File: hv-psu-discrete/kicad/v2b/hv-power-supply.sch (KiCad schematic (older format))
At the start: 86 parts, among them J1 AC-HV, J10 GND_LV, J11 EARTH, J12 AC-LV, J13 AC-LV, J2 AC-HV, J3 HV, J4 GND_HV, J5 LV, J6 GND_LV, J7 LED, J8 GND_LV, J9 +5V, Q1 LND150N3-G, Q2 IRF840, Q3 MMBT3904, U1 LT3080xT, U2 LM317_TO-220, U3 LM7805_TO220, U4 TLC555xD

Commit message: WIP
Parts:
- removed C8, C9: 10nF/50V, Capacitor_SMD:C_0805_2012Metric_Pad1.18x1.45mm_HandSolder, symbol Device:C
- removed D1: BYG20J, Diode_SMD:D_SMA_Handsoldering, symbol Device:D
- removed D14: 1N4148W, Diode_SMD:D_SOD-123, symbol Diode:1N4148W
- removed RL1: G2RL-2-DC5, Relay_THT:Relay_DPDT_Omron_G2RL, symbol Relay:G2RL-2-DC5
- removed U1: LT3080xT, Package_TO_SOT_THT:TO-220-5_P3.4x3.7mm_StaggerOdd_Lead3.8mm_Vertical, symbol Regulator_Linear:LT3080xT
- added D1: 1N4148W, Diode_SMD:D_SOD-123, symbol Diode:1N4148W
- added D14: BYG20J, Diode_SMD:D_SMA_Handsoldering, symbol Device:D
- added D17, D18: 1N4007, Diode_SMD:D_SMA_Handsoldering, symbol Diode:1N4007
- added K1: G6S-2 DC5, Relay_THT:Relay_DPDT_Omron_G6S-2, symbol Relay:G6S-2
- added R19: Rs/2W, Resistor_THT:R_Axial_DIN0414_L11.9mm_D4.5mm_P15.24mm_Horizontal, symbol Device:R
- added R20: Rs/0.6W, Resistor_THT:R_Axial_DIN0207_L6.3mm_D2.5mm_P10.16mm_Horizontal, symbol Device:R
- added R21, R22: 100k/2W, Resistor_THT:R_Axial_DIN0414_L11.9mm_D4.5mm_P15.24mm_Horizontal, symbol Device:R
- added U1: LT3080xST, Package_TO_SOT_SMD:SOT-223, symbol Regulator_Linear:LT3080xST
- C1: value 2.2nF/2kV -> Cx/10nF/50V; footprint Capacitor_THT:C_Rect_L18.0mm_W5.0mm_P15.00mm_FKS3_FKP3 -> Capacitor_SMD:C_0805_2012Metric_Pad1.18x1.45mm_HandSolder
- C14: footprint Capacitor_THT:CP_Radial_D30.0mm_P10.00mm_SnapIn -> Capacitor_THT:CP_Radial_D35.0mm_P10.00mm_SnapIn
- C2: value 10nF/630VDC -> 2.2nF 2kV; footprint Capacitor_THT:C_Rect_L13.0mm_W4.0mm_P10.00mm_FKS3_FKP3_MKS4 -> Capacitor_THT:C_Rect_L18.0mm_W5.0mm_P15.00mm_FKS3_FKP3
- C20: footprint Capacitor_Tantalum_SMD:CP_EIA-7343-31_Kemet-D_Pad2.25x2.55mm_HandSolder -> Capacitor_Tantalum_SMD:CP_EIA-3216-12_Kemet-S_Pad1.58x1.35mm_HandSolder
- C3: value 10nF/630VDC -> Cs/50V; footprint Capacitor_THT:C_Rect_L13.0mm_W4.0mm_P10.00mm_FKS3_FKP3_MKS4 -> Capacitor_SMD:C_0805_2012Metric_Pad1.18x1.45mm_HandSolder
- C4: value 10nF/50V -> Cx/10nF/630V; footprint Capacitor_SMD:C_0805_2012Metric_Pad1.18x1.45mm_HandSolder -> Capacitor_THT:C_Rect_L13.0mm_W4.0mm_P10.00mm_FKS3_FKP3_MKS4
- C5: value 10nF/50V -> Cs/630V; footprint Capacitor_SMD:C_0805_2012Metric_Pad1.18x1.45mm_HandSolder -> Capacitor_THT:C_Rect_L18.0mm_W5.0mm_P15.00mm_FKS3_FKP3
- C6: value 10nF/630VDC -> 100nF/50V; footprint Capacitor_THT:C_Rect_L13.0mm_W4.0mm_P10.00mm_FKS3_FKP3_MKS4 -> Capacitor_SMD:C_0805_2012Metric_Pad1.18x1.45mm_HandSolder
- C7: value 10nF/630VDC -> 100nF/630V; footprint Capacitor_THT:C_Rect_L13.0mm_W4.0mm_P10.00mm_FKS3_FKP3_MKS4 -> Capacitor_THT:C_Rect_L18.0mm_W5.0mm_P15.00mm_FKS3_FKP3
- D10, D9: value 1N4736A/6.3V -> MMSZ5234BT1G/6.2V; footprint Diode_THT:D_DO-41_SOD81_P10.16mm_Horizontal -> Diode_SMD:D_SOD-123
- D11, D15: footprint Diode_THT:D_DO-41_SOD81_P10.16mm_Horizontal -> Diode_SMD:D_SMA_Handsoldering
- D12: value 1N4007 -> 1N4148W; footprint Diode_THT:D_DO-41_SOD81_P10.16mm_Horizontal -> Diode_SMD:D_SOD-123
- D16: value 1N4747A/20V -> MMSZ20T1G/20V; footprint Diode_THT:D_DO-41_SOD81_P10.16mm_Horizontal -> Diode_SMD:D_SOD-123
- D2, D5: value BYG20J -> BYG22B-E3
- D3, D4: value BYV98-200 -> BYG22B-E3; footprint kicad-snk:SOD64-10 -> Diode_SMD:D_SMA_Handsoldering
- D7, D8: value BYV98-200 -> BYG20J; footprint kicad-snk:SOD64-10 -> Diode_SMD:D_SMA_Handsoldering
- HS1: footprint Heatsink:Heatsink_Fischer_SK104-STC-STIC_35x13mm_2xDrill2.5mm -> Heatsink:Heatsink_Fischer_SK129-STS_42x25mm_2xDrill2.5mm
- J1, J2: value AC-HV -> AC-LV
- J11: value EARTH -> AC-HV
- J12: value AC-LV -> AC-HV
- J13: value AC-LV -> EARTH
- Q1: footprint Package_TO_SOT_THT:TO-92 -> Package_TO_SOT_SMD:SOT-89-3_Handsoldering
- R1: value 100R/2W -> Rs/1/8W; footprint Resistor_THT:R_Axial_DIN0411_L9.9mm_D3.6mm_P15.24mm_Horizontal -> Resistor_SMD:R_0805_2012Metric_Pad1.20x1.40mm_HandSolder
- R18: footprint Resistor_THT:R_Axial_DIN0411_L9.9mm_D3.6mm_P15.24mm_Horizontal -> Resistor_THT:R_Axial_DIN0414_L11.9mm_D4.5mm_P15.24mm_Horizontal
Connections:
- net GND_HV: now also C7.2, D6.2 (A), D7.2 (A), R18.2, D18.2 (A), R21.2, R22.2; no longer C1.1, C3.1, D2.2 (A), R1.1
- net GND_LV: now also C6.2, D2.2 (A); no longer C4.2, C5.1, D4.2 (A)
- net at C4.1, J12.1 (Pin_1): now also K1.8, R19.2; no longer D3.1 (K), D7.2 (A)
- net at C14.1, C15.1, C16.1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: now also D4.1 (K), D5.1 (K); no longer D7.1 (K), D8.1 (K)
- net at C10.1, C11.1, D15.1 (K)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: now also D8.1 (K), D14.1 (K); no longer C6.2, C7.1, D5.1 (K), D6.1 (K)
- net at C1.2, R1.2: now also D3.1 (K), D5.2 (A), J2.1 (Pin_1), R20.2; no longer J11.1 (Pin_1)
- net at J3.1 (Pin_1): now also C23.1, D10.2 (A), D15.2 (A), D16.2 (A), R6.2, D17.1 (K), D18.1 (K), R21.1, R22.1, U1.2 (OUT), U1.4 (OUT)
- net at C12.1, D16.1 (K), D9.2 (A)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: now also U1.3 (IN)
- net at C13.2, R5.1, R6.1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: now also C7.1, D17.2 (A)
- net at C13.1, R5.2: now also U1.1 (SET)
- net at C19.1, D11.2 (A), D12.1 (K)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: now also C6.1
- net at R18.1: now also C2.1, J13.1 (Pin_1)
- net +5VDC: now reaches C18.1, C20.1, C22.1, J9.1 (Pin_1), R15.2, U3.3 (VO), U4.4 (R), U4.6 (THR), U4.8 (VCC)
- net +5VDC: now also D1.1 (K), K1.1
- net RELCTRL: now reaches Q3.3 (C)
- net RELCTRL: now also D1.2 (A), K1.12
- new net: C1.1, C3.1, D2.1 (K), D4.2 (A), J1.1 (Pin_1)
- new net: C3.2, R1.1, R20.1
- new net: D6.1 (K), D8.2 (A), K1.9
- new net: D14.2 (A), D7.1 (K), K1.4
- new net: C4.2, C5.2, J11.1 (Pin_1), K1.5
- new net: C5.1, R19.1
- no-connect marks 2 -> 3
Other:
- note added: "13,4°/W"
- note added: "3.7°/W"
- note added: "Cs=100nF/50V\nRs=22R/0.6W"
- note added: "Cs=100nF/630V\nRs=470R/0.6W"
- note added: "Snubber"
- moved on the sheet: C19, J3, J4, J5, J6

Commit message: WIP
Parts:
- Q1: footprint Package_TO_SOT_SMD:SOT-89-3_Handsoldering -> Package_TO_SOT_SMD:SOT-89-3
- R6: value 1k/2W -> 1k/0.6W
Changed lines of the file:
@@
 F 0 "Q1" V 8492 3050 50  0000 C CNN
 F 1 "LND150N3-G" V 8401 3050 50  0000 C CNN
-F 2 "Package_TO_SOT_SMD:SOT-89-3_Handsoldering" H 8350 3150 50  0001 C CNN
+F 2 "Package_TO_SOT_SMD:SOT-89-3" H 8350 3150 50  0001 C CNN
 F 3 "~" H 8150 3050 50  0001 C CNN
 	1    8150 3050
@@
 P 12350 3350
 F 0 "R6" H 12280 3304 50  0000 R CNN
-F 1 "1k/2W" H 12280 3395 50  0000 R CNN
+F 1 "1k/0.6W" H 12280 3395 50  0000 R CNN
 F 2 "Resistor_THT:R_Axial_DIN0207_L6.3mm_D2.5mm_P10.16mm_Horizontal" V 12280 3350 50  0001 C CNN
 F 3 "~" H 12350 3350 50  0001 C CNN

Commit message: layout completed
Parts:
- C20: value 15uF/25V -> 15uF/10V
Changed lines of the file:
@@
 Sheet 1 1
 Title "HV Power Supply"
-Date "2021-09-01"
+Date "2021-09-02"
 Rev "2b"
 Comp ""
@@
 P 9600 6600
 F 0 "C20" H 9718 6646 50  0000 L CNN
-F 1 "15uF/25V" H 9718 6555 50  0000 L CNN
+F 1 "15uF/10V" H 9718 6555 50  0000 L CNN
 F 2 "Capacitor_Tantalum_SMD:CP_EIA-3216-12_Kemet-S_Pad1.58x1.35mm_HandSolder" H 9638 6450 50  0001 C CNN
 F 3 "~" H 9600 6600 50  0001 C CNN

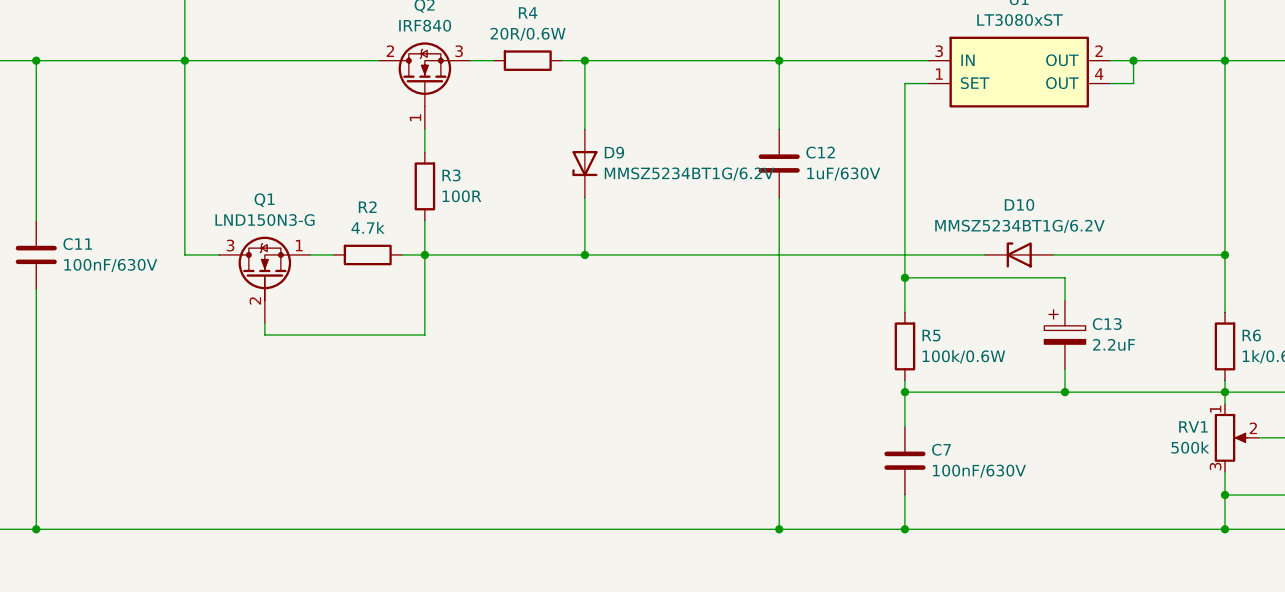
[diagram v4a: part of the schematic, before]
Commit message: Update hv-power-supply.sch
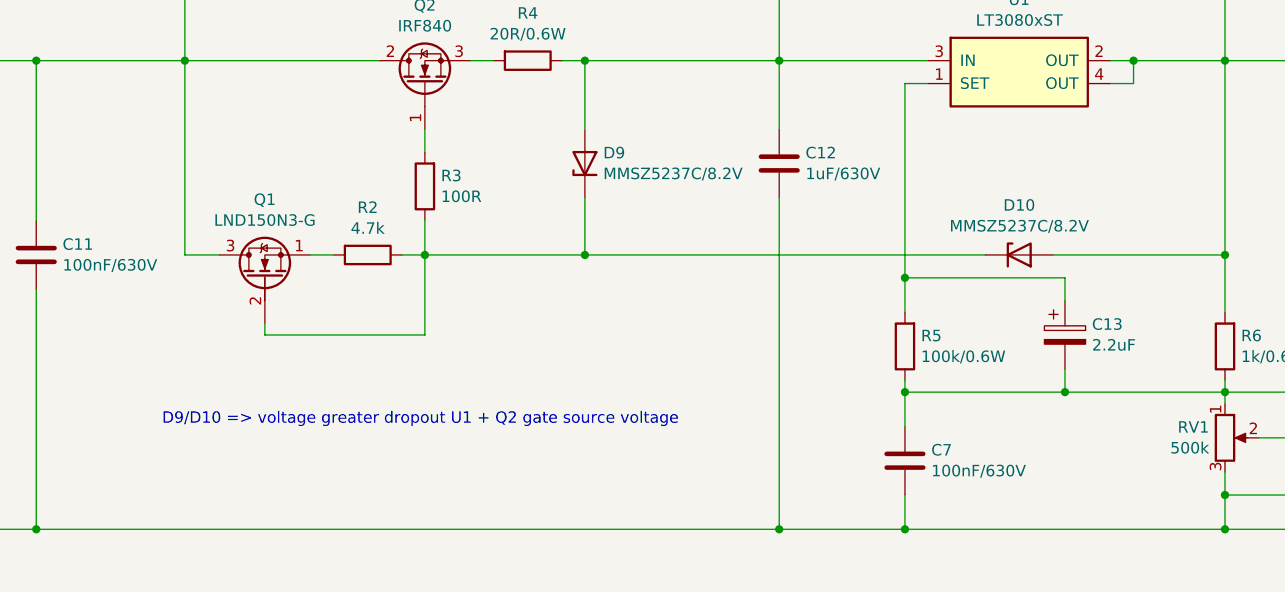
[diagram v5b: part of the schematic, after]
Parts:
- D10, D9: value MMSZ5234BT1G/6.2V -> MMSZ5237C/8.2V
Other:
- note added: "D9/D10 => voltage greater dropout U1 + Q2 gate source voltage"
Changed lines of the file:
@@
 Sheet 1 1
 Title "HV Power Supply"
-Date "2021-09-02"
+Date "2021-09-19"
 Rev "2b"
 Comp ""
@@
 P 9550 2550
 F 0 "D9" V 9596 2470 50  0000 R CNN
-F 1 "MMSZ5234BT1G/6.2V" V 9505 2470 50  0000 R CNN
+F 1 "MMSZ5237C/8.2V" V 9505 2470 50  0000 R CNN
 F 2 "Diode_SMD:D_SOD-123" H 9550 2375 50  0001 C CNN
 F 3 "" H 9550 2550 50  0001 C CNN
@@
 P 11450 2950
 F 0 "D10" H 11450 3167 50  0000 C CNN
-F 1 "MMSZ5234BT1G/6.2V" H 11450 3076 50  0000 C CNN
+F 1 "MMSZ5237C/8.2V" H 11450 3076 50  0000 C CNN
 F 2 "Diode_SMD:D_SOD-123" H 11450 2775 50  0001 C CNN
 F 3 "" H 11450 2950 50  0001 C CNN
@@
 Text Notes 8000 5500 0    50   ~ 0
 13,4°/W
+Text Notes 7700 3700 0    50   ~ 0
+D9/D10 => voltage greater dropout U1 + Q2 gate source voltage
 $EndSCHEMATC
